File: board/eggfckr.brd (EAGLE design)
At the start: 91.1 x 30.5 mm, 8 parts, among them U1 ATTINY85-20PU

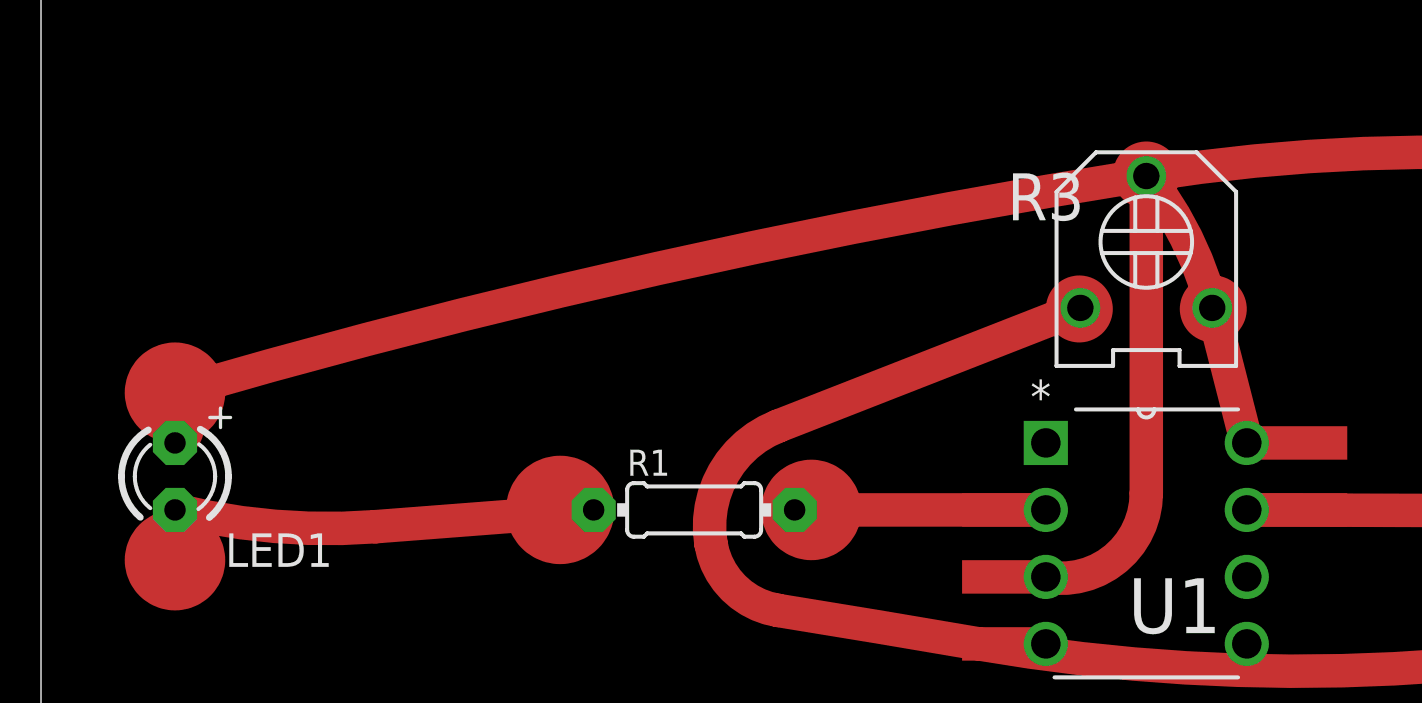
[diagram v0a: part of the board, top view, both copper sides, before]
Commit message: flipped LEDon pin2
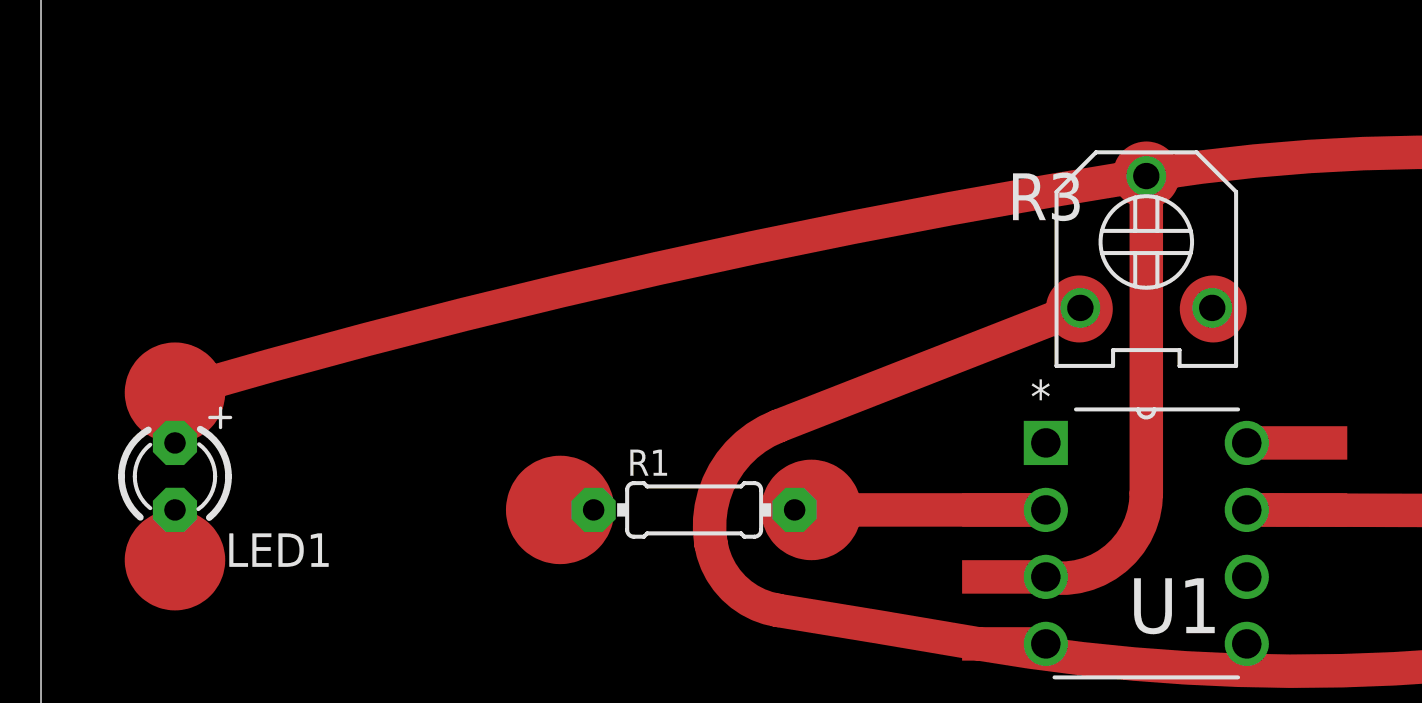
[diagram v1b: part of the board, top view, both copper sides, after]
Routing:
- net N$3: track 15.9 -> 0.00 mm
- net VCC: track 98.7 -> 86.5 mm
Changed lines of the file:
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@@
 <wire x1="55.217921875" y1="10.132921875" x2="45.72" y2="10.16" width="1.27" layer="1"/>
-</signal>
-<signal name="N$6">
-<contactref element="R1" pad="1"/>
-<contactref element="LED1" pad="K"/>
-<wire x1="20.955" y1="10.16" x2="12.7" y2="9.525" width="1.27" layer="1"/>
-<wire x1="12.7" y1="9.525" x2="5.08" y2="10.16" width="1.27" layer="1" curve="-18.324694"/>
 </signal>
 <signal name="N$7">
@@
 <signal name="VCC">
 <contactref element="LED2" pad="A"/>
-<contactref element="LED1" pad="A"/>
-<contactref element="U1" pad="8"/>
-<contactref element="R3" pad="3"/>
-<wire x1="44.41" y1="17.82" x2="44.57455" y2="17.17686875" width="1.27" layer="1"/>
 <contactref element="VCC" pad="1"/>
-<wire x1="44.57455" y1="17.17686875" x2="45.72" y2="12.7" width="1.27" layer="1"/>
 <wire x1="87.63" y1="12.7" x2="77.47" y2="13.97" width="1.27" layer="1"/>
 <wire x1="77.47" y1="13.97" x2="71.12" y2="17.78" width="1.27" layer="1" curve="-25.716182"/>
@@
 <wire x1="41.91" y1="22.86" x2="5.08" y2="14.605" width="1.27" layer="1" curve="7.189045"/>
 <wire x1="5.08" y1="14.605" x2="5.08" y2="13.97" width="1.27" layer="1" curve="147.544393"/>
-<wire x1="5.08" y1="13.97" x2="5.08" y2="12.7" width="1.27" layer="1" curve="-147.544393"/>
-<wire x1="44.41" y1="17.82" x2="41.91" y2="22.86" width="1.27" layer="1" curve="24.062389"/>
+<contactref element="LED1" pad="A"/>
+<contactref element="R3" pad="3"/>
+<contactref element="U1" pad="8"/>
+<wire x1="45.72" y1="12.7" x2="44.41" y2="17.82" width="0" layer="19" extent="1-1"/>
+<wire x1="41.91" y1="22.86" x2="44.41" y2="17.82" width="0" layer="19" extent="1-1"/>
+<wire x1="5.08" y1="12.7" x2="5.08" y2="13.97" width="0" layer="19" extent="1-1"/>
 </signal>
 <signal name="N$4">
@@
 <wire x1="41.91" y1="10.795" x2="38.1" y2="7.62" width="1.27" layer="1" curve="-100.388876"/>
 </signal>
+<signal name="N$3">
+<contactref element="R1" pad="1"/>
+<contactref element="LED1" pad="K"/>
+<wire x1="5.08" y1="10.16" x2="20.955" y2="10.16" width="0" layer="19" extent="1-1"/>
+</signal>
 </signals>

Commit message: changed routing
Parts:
- removed R3: (no value), dp_devices:TRIMMER_3306F
- added S1: SWITCH-MOMENTARY-2-SMD-1101NE, ATtami:TACTILE-SWITCH-1101NE
- moved VCC 45.2 mm to (28.6, 2.54), turned to 270 degrees
- moved LED2 41.9 mm to (45.7, 12.1)
- moved GND 39.6 mm to (26.0, 2.54), turned to 270 degrees
- moved R2 20.0 mm to (38.0, 10.8), turned to 180 degrees
- moved U1 14.6 mm to (31.1, 5.71)
- moved R1 8.47 mm to (16.5, 8.26)
- moved LED1 5.12 mm to (7.62, 6.99)
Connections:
- new net N$5: S1.P$1, U1.2
- net GND: now also LED1.K; no longer R3.1
- net N$2: now also R1.2; no longer R3.2
- net N$3: now also LED1.A; no longer LED1.K
- net N$4: now also S1.P$2, U1.1; no longer R1.2, U1.2
- net VCC: no longer LED1.A, R3.3
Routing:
- net VCC: track 86.5 -> 0.00 mm
- net GND: track 58.9 -> 0.00 mm
- net N$7: track 30.4 -> 0.00 mm
- net N$2: track 17.0 -> 0.00 mm
- net N$4: track 9.53 -> 0.00 mm
- net N$1: track 9.50 -> 0.00 mm
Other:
- board size 91.1 x 30.5 mm -> 53.6 x 21.6 mm

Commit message: dual
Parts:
- removed GND, VCC: (no value), microbuilder:1X01_ROUND
- added BATT1: FKIT-COIN_CELLLIR2450-H, SparkFun-Electromechanical:FKIT-LIR2450-H
- added JP1: (no value), SparkFun-Connectors:STEREOJACK2.5MM_SPECIA_POGOPINS
- added RV1: (no value), SparkFun-Electromechanical:POT_ALPHA_RV16AF-20
- added U2: ATTINY85-20PU, Atmel_By_element14_Batch_1-00:DIP254P762X533-8
- S1: value SWITCH-MOMENTARY-2-SMD-1101NE -> (none); device ATtami:TACTILE-SWITCH-1101NE -> adafruit:EG1218
- moved R2 40.3 mm to (78.1, 7.62), turned to 0 degrees
- moved R1 22.9 mm to (39.4, 8.26)
- moved LED2 12.8 mm to (57.1, 6.35)
- moved LED1 7.62 mm to (15.2, 6.99)
- moved S1 2.69 mm to (26.0, 19.7)
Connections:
- new net N$6: LED2.A, U2.3
- new net N$8: BATT1.NEG, S1.S
- net GND: now also BATT1.POS, JP1.RING1, LED2.K, RV1.3, U2.4; no longer GND.1
- net N$1: now also R1.1, U1.6; no longer R2.2, U1.7
- net N$2: now also LED1.A; no longer R1.2
- net N$3: now also JP1.SHIELD, R1.2; no longer LED1.A, R1.1
- net N$4: now also RV1.2, U1.7, U2.7; no longer S1.P$2, U1.1
- net N$5: now also R2.1, U2.6; no longer S1.P$1, U1.2
- net N$7: now also JP1.TIP, R2.2; no longer LED2.K, R2.1
- net VCC: now also RV1.1, S1.P, U2.8; no longer LED2.A, VCC.1
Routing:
- net GND: track 0.00 -> 132.1 mm
- net VCC: track 0.00 -> 57.9 mm
- net N$3: track 0.00 -> 51.8 mm
- net N$4: track 0.00 -> 48.1 mm
- net N$8: track 0.00 -> 41.3 mm
- net N$2: track 0.00 -> 9.15 mm
- net N$7: track 0.00 -> 8.91 mm
- net N$6: track 0.00 -> 5.72 mm
- net N$1: track 0.00 -> 4.45 mm
- net N$5: track 0.00 -> 3.81 mm
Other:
- board size 53.6 x 21.6 mm -> 114 x 26.7 mm

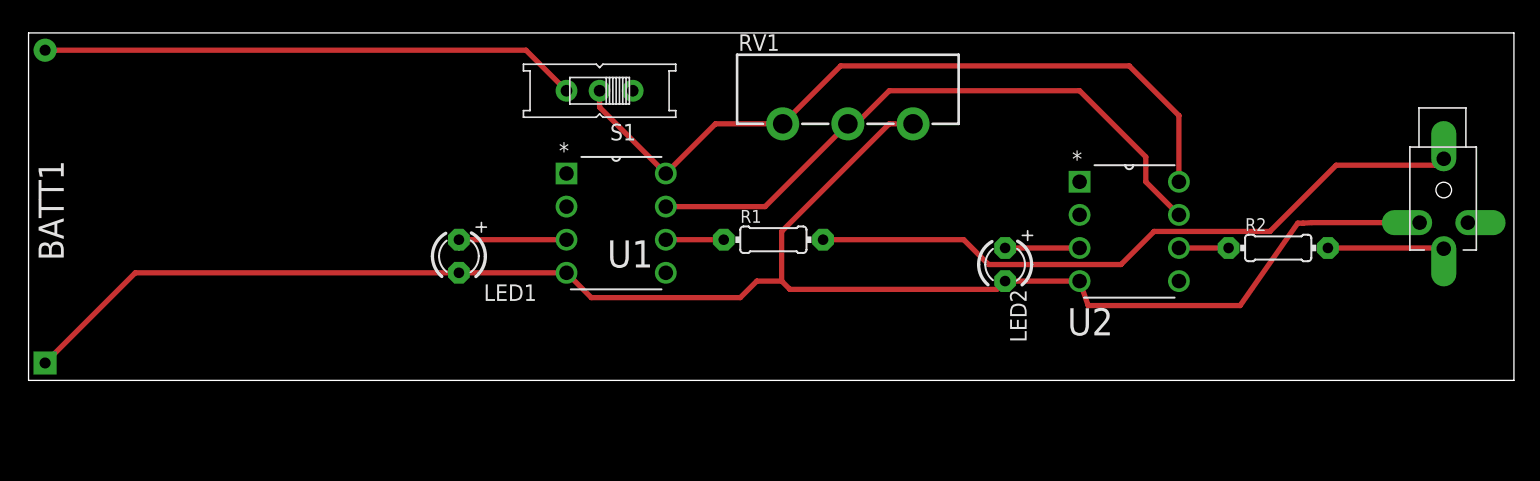
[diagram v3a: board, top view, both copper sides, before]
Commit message: flipped attiny85
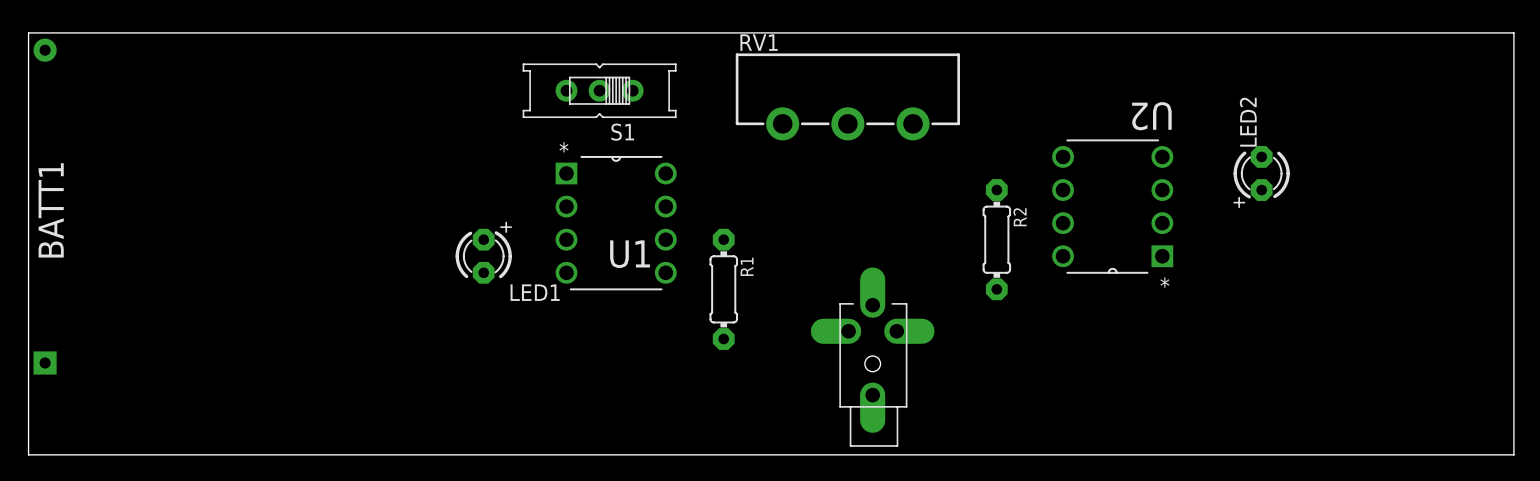
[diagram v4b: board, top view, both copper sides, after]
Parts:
- moved JP1 45.8 mm to (47.0, -1.27), turned to 90 degrees
- moved R2 21.6 mm to (56.5, 8.26), turned to 270 degrees
- moved LED2 20.9 mm to (76.8, 13.3), turned to 90 degrees
- moved U2 13.0 mm to (61.6, 14.6), turned to 180 degrees
- moved R1 5.39 mm to (35.6, 4.45), turned to 270 degrees
- moved LED1 1.90 mm to (17.1, 6.99)
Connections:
- net N$3: now also JP1.TIP; no longer JP1.SHIELD
- net N$7: now also JP1.SHIELD; no longer JP1.TIP
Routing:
- net GND: track 132.1 -> 0.00 mm
- net VCC: track 57.9 -> 0.00 mm
- net N$3: track 51.8 -> 0.00 mm
- net N$4: track 48.1 -> 0.00 mm
- net N$8: track 41.3 -> 0.00 mm
- net N$2: track 9.15 -> 0.00 mm
- net N$7: track 8.91 -> 0.00 mm
- net N$6: track 5.72 -> 0.00 mm
- net N$1: track 4.45 -> 0.00 mm
- net N$5: track 3.81 -> 0.00 mm
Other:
- board size 114 x 26.7 mm -> 114 x 32.4 mm

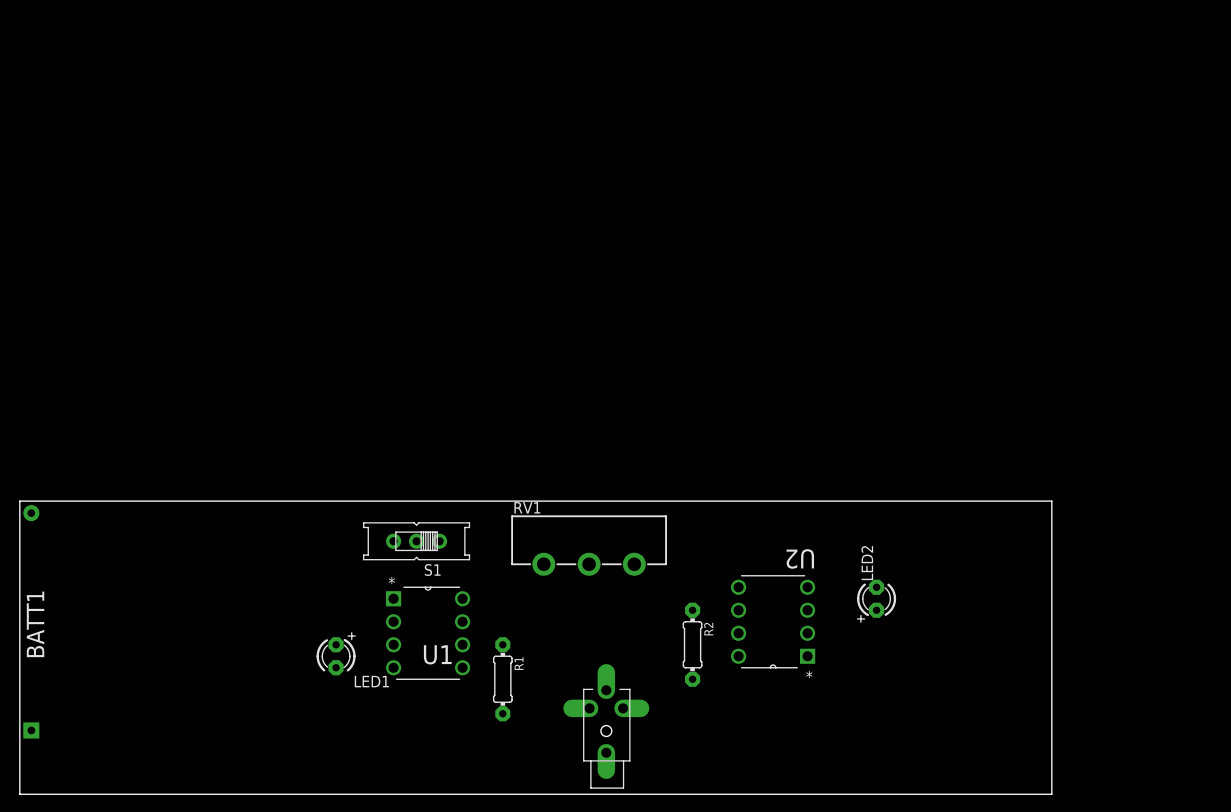
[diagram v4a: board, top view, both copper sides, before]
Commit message: library and split processors
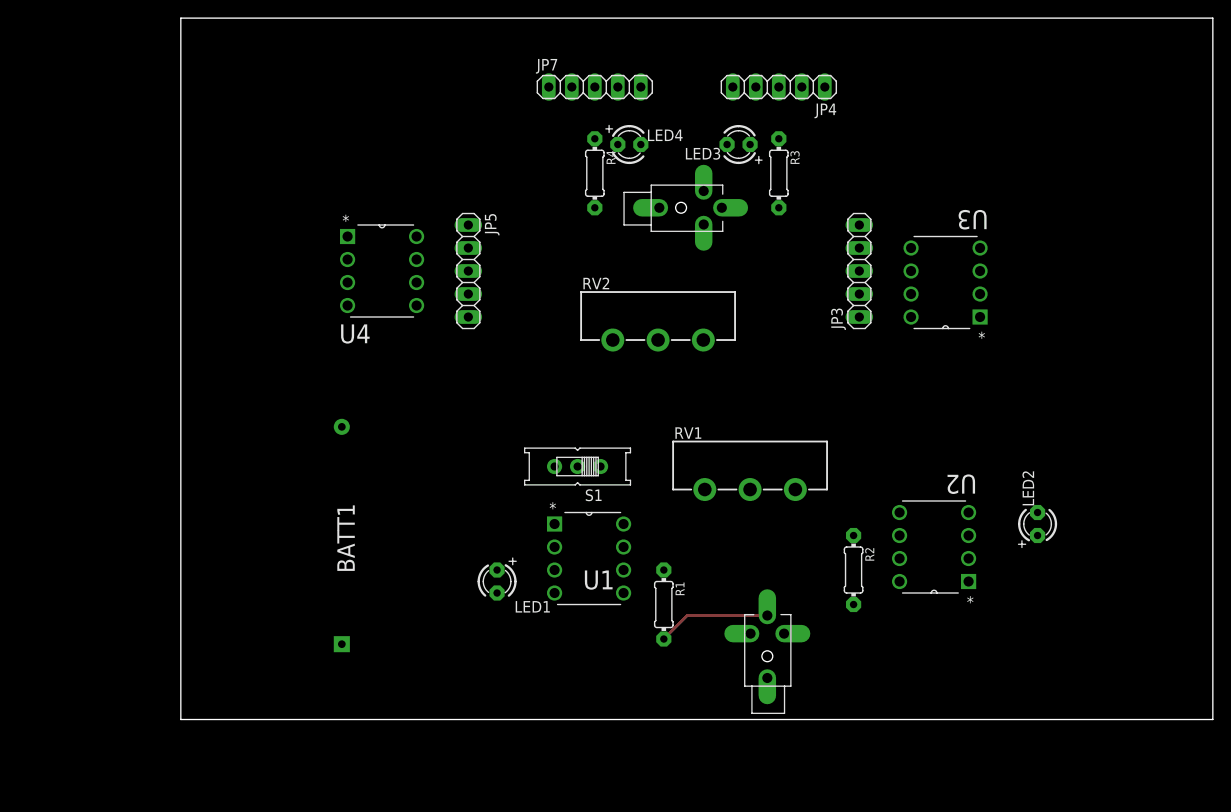
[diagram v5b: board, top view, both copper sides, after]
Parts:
- added JP2: (no value), SparkFun-Connectors:STEREOJACK2.5MM_SPECIA_POGOPINS
- added JP3, JP4, JP5, JP7: (no value), eggfckr:1X05
- added LED3, LED4: (no value), adafruit:LED3MM
- added R3, R4: (no value), adafruit:0204/7
- added RV2: (no value), SparkFun-Electromechanical:POT_ALPHA_RV16AF-20
- added U3, U4: ATTINY85-20PU, Atmel_By_element14_Batch_1-00:DIP254P762X533-8
- moved BATT1 35.6 mm to (17.8, 20.3)
- moved U1 19.6 mm to (48.9, 14.0)
- moved LED2 19.6 mm to (94.6, 21.6)
- moved R1 19.6 mm to (53.3, 12.7)
- moved R2 19.6 mm to (74.3, 16.5)
- moved RV1 19.6 mm to (62.9, 25.4)
- moved S1 19.6 mm to (43.8, 27.9)
- moved U2 19.6 mm to (79.4, 22.9)
- moved JP1 19.6 mm to (64.8, 6.99)
- moved LED1 19.6 mm to (34.9, 15.2)
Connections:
- new net N$10: JP3.4, U3.3
- new net N$11: JP4.2, JP7.2, RV2.2
- new net N$12: JP7.3, R4.1
- new net N$13: JP4.4, LED3.A
- new net N$14: JP5.4, U4.3
- new net N$15: JP2.SHIELD, R4.2
- new net N$16: JP2.TIP, R3.2
- new net N$17: JP3.1, U3.8
- new net N$18: JP3.3, U3.6
- new net N$19: JP3.2, U3.7
- new net N$20: JP3.5, U3.4
- new net N$21: JP5.1, U4.8
- new net N$22: JP5.3, U4.6
- new net N$23: JP5.2, U4.7
- new net N$24: JP5.5, U4.4
- new net N$30: JP7.4, LED4.A
- new net N$9: JP4.3, R3.1
- net GND: now also JP2.RING1, JP4.5, JP7.5, LED3.K, LED4.K, RV2.3
- net VCC: now also JP4.1, JP7.1, RV2.1
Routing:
- net N$3: track 0.00 -> 12.5 mm
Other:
- board size 114 x 32.4 mm -> 114 x 77.5 mm

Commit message: getting ready for svg2snhn
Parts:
- removed JP2: (no value), SparkFun-Connectors:STEREOJACK2.5MM_SPECIA_POGOPINS
- removed JP3, JP4, JP5, JP7: (no value), eggfckr:1X05
- removed LED3, LED4: (no value), adafruit:LED3MM
- removed R3, R4: (no value), adafruit:0204/7
- removed RV2: (no value), SparkFun-Electromechanical:POT_ALPHA_RV16AF-20
- removed U3, U4: ATTINY85-20PU, Atmel_By_element14_Batch_1-00:DIP254P762X533-8
- moved LED1 33.0 mm to (3.17, 24.1)
- moved S1 15.7 mm to (33.0, 16.5), turned to 90 degrees
- moved LED2 12.3 mm to (106.7, 24.1)
- moved BATT1 6.02 mm to (15.9, 14.6), turned to 180 degrees
- moved R1 4.49 mm to (54.0, 17.1), turned to 0 degrees
- moved RV1 4.49 mm to (63.5, 21.0)
- moved U2 4.49 mm to (82.5, 19.7)
- moved U1 2.29 mm to (47.6, 12.1)
- moved JP1 2.29 mm to (63.5, 8.89)
- moved R2 0.90 mm to (73.7, 17.1), turned to 180 degrees
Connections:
- removed net N$10: JP3.4, U3.3
- removed net N$11: JP4.2, JP7.2, RV2.2
- removed net N$12: JP7.3, R4.1
- removed net N$13: JP4.4, LED3.A
- removed net N$14: JP5.4, U4.3
- removed net N$15: JP2.SHIELD, R4.2
- removed net N$16: JP2.TIP, R3.2
- removed net N$17: JP3.1, U3.8
- removed net N$18: JP3.3, U3.6
- removed net N$19: JP3.2, U3.7
- removed net N$20: JP3.5, U3.4
- removed net N$21: JP5.1, U4.8
- removed net N$22: JP5.3, U4.6
- removed net N$23: JP5.2, U4.7
- removed net N$24: JP5.5, U4.4
- removed net N$30: JP7.4, LED4.A
- removed net N$9: JP4.3, R3.1
- net GND: no longer JP2.RING1, JP4.5, JP7.5, LED3.K, LED4.K, RV2.3
- net VCC: no longer JP4.1, JP7.1, RV2.1
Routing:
- net N$3: track 12.5 -> 0.00 mm
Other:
- board size 114 x 77.5 mm -> 114 x 28.6 mm
